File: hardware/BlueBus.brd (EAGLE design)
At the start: 90 x 55 mm, 75 parts, among them Y1 32.768kHz

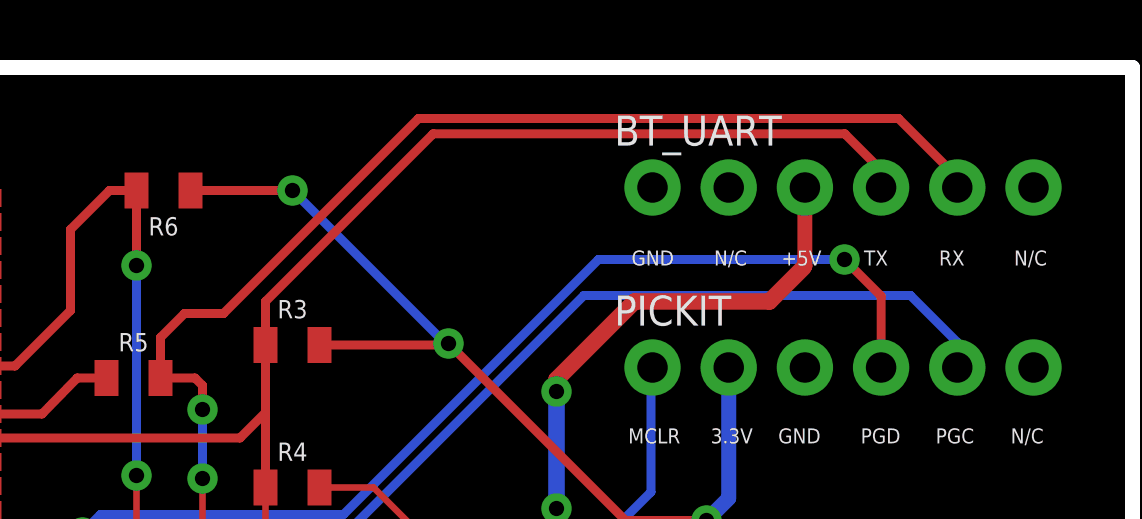
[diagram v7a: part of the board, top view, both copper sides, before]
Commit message: [ADD] hardware: BT_UART I/O Change * Re-wire BT_UART for FTDI cable compatability
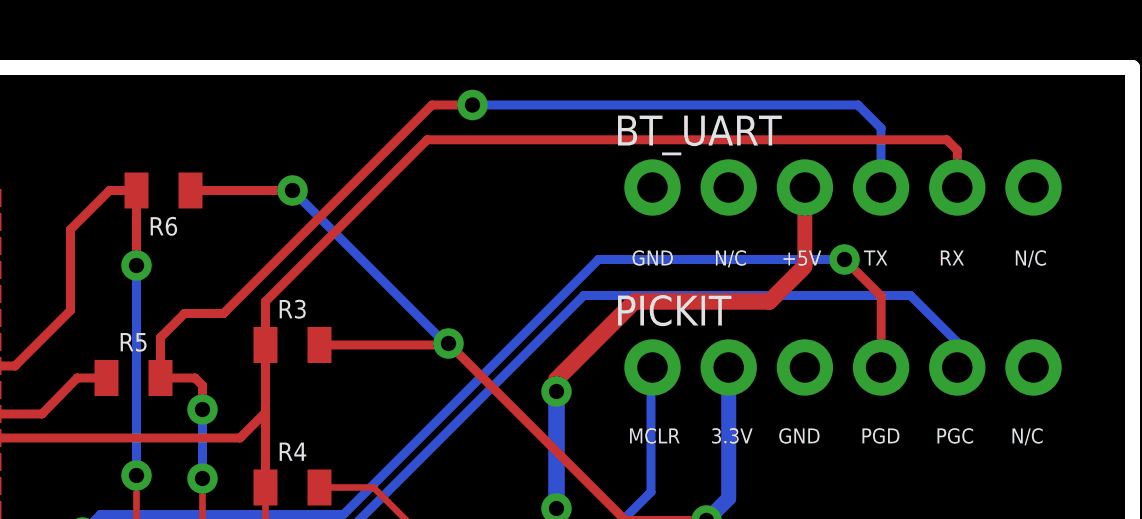
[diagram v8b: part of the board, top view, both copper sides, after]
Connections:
- net BT_URX: now also BT_UART.4; no longer BT_UART.5
- net BT_UTX: now also BT_UART.5; no longer BT_UART.4
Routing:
- net BT_UTX: track 62.3 -> 65.0 mm
- net BT_URX: track 63.4 -> 62.2 mm, vias 2 -> 3
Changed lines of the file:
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@@
 <wire x1="61.1" y1="45.75" x2="61.1" y2="43.5" width="0.3" layer="1"/>
 <wire x1="61.1" y1="43.5" x2="61.1" y2="41" width="0.3" layer="1"/>
-<wire x1="66.69" y1="52.79" x2="61.1" y2="47.2" width="0.3" layer="1"/>
+<wire x1="61.1" y1="47.2" x2="66.49" y2="52.59" width="0.3" layer="1"/>
 <wire x1="61.1" y1="47.2" x2="61.1" y2="45.75" width="0.3" layer="1"/>
-<wire x1="66.69" y1="52.79" x2="80.41" y2="52.79" width="0.3" layer="1"/>
+<wire x1="83.81" y1="52.59" x2="66.49" y2="52.59" width="0.3" layer="1"/>
 <wire x1="48.25" y1="25.1" x2="48.25" y2="26.45" width="0.22" layer="1"/>
 <wire x1="51.1" y1="27.1" x2="48.9" y2="27.1" width="0.22" layer="1"/>
@@
 <wire x1="51.8" y1="42.65" x2="60.25" y2="42.65" width="0.3" layer="1"/>
 <wire x1="60.25" y1="42.65" x2="61.1" y2="43.5" width="0.3" layer="1"/>
-<contactref element="BT_UART" pad="4"/>
-<wire x1="80.41" y1="52.79" x2="81.62" y2="51.58" width="0.3" layer="1"/>
-<wire x1="81.62" y1="51.58" x2="81.62" y2="51" width="0.3" layer="1"/>
+<contactref element="BT_UART" pad="5"/>
+<wire x1="84.16" y1="51" x2="84.16" y2="52.24" width="0.3" layer="1"/>
+<wire x1="84.16" y1="52.24" x2="83.81" y2="52.59" width="0.3" layer="1"/>
 </signal>
 <signal name="BT_URX">
@@
 <contactref element="BC127" pad="42"/>
 <contactref element="R5" pad="1"/>
-<wire x1="66.2" y1="53.3" x2="82.2" y2="53.3" width="0.3" layer="1"/>
 <wire x1="51.8" y1="43.45" x2="53.65" y2="43.45" width="0.3" layer="1"/>
 <wire x1="53.65" y1="43.45" x2="54.8239125" y2="44.65" width="0.3" layer="1"/>
@@
 <wire x1="59" y1="43.6" x2="59" y2="41.3" width="0.3" layer="16"/>
 <via x="59" y="41.3" extent="1-16" drill="0.508"/>
-<wire x1="66.2" y1="53.3" x2="59.7" y2="46.8" width="0.3" layer="1"/>
-<wire x1="59.7" y1="46.8" x2="58.4" y2="46.8" width="0.3" layer="1"/>
+<wire x1="58.4" y1="46.8" x2="59.7" y2="46.8" width="0.3" layer="1"/>
 <wire x1="58.4" y1="46.8" x2="57.6" y2="46" width="0.3" layer="1"/>
 <wire x1="57.6" y1="46" x2="57.6" y2="44.65" width="0.3" layer="1"/>
-<contactref element="BT_UART" pad="5"/>
-<wire x1="82.2" y1="53.3" x2="84.16" y2="51.34" width="0.3" layer="1"/>
-<wire x1="84.16" y1="51.34" x2="84.16" y2="51" width="0.3" layer="1"/>
+<contactref element="BT_UART" pad="4"/>
+<wire x1="68" y1="53.75" x2="66.65" y2="53.75" width="0.3" layer="1"/>
+<via x="68" y="53.75" extent="1-16" drill="0.51"/>
+<wire x1="80.85" y1="53.75" x2="68" y2="53.75" width="0.3" layer="16"/>
+<wire x1="81.62" y1="52.98" x2="81.62" y2="51" width="0.3" layer="16"/>
+<wire x1="59.7" y1="46.8" x2="66.65" y2="53.75" width="0.3" layer="1"/>
+<wire x1="80.85" y1="53.75" x2="81.62" y2="52.98" width="0.3" layer="16"/>
 <wire x1="57.6" y1="44.65" x2="55.8" y2="44.65" width="0" layer="19" extent="1-1"/>
 </signal>
